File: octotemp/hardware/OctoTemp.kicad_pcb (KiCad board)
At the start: 2 copper layers, 50.5 x 37 mm, 48 parts, among them U1 ESP-12E, U2 SPX3819M5, U3 ADC128D818

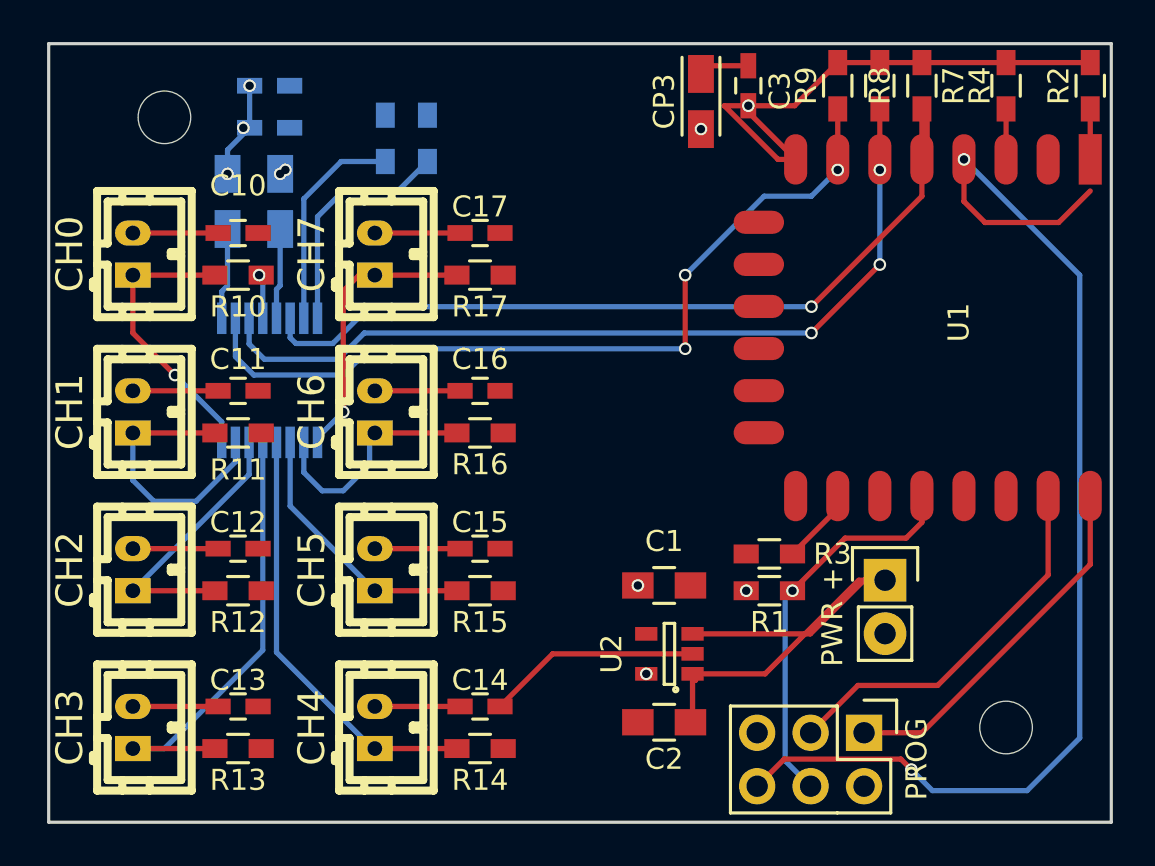
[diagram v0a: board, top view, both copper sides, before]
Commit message: Rearrange board to fit properly in Hammond 1551L.
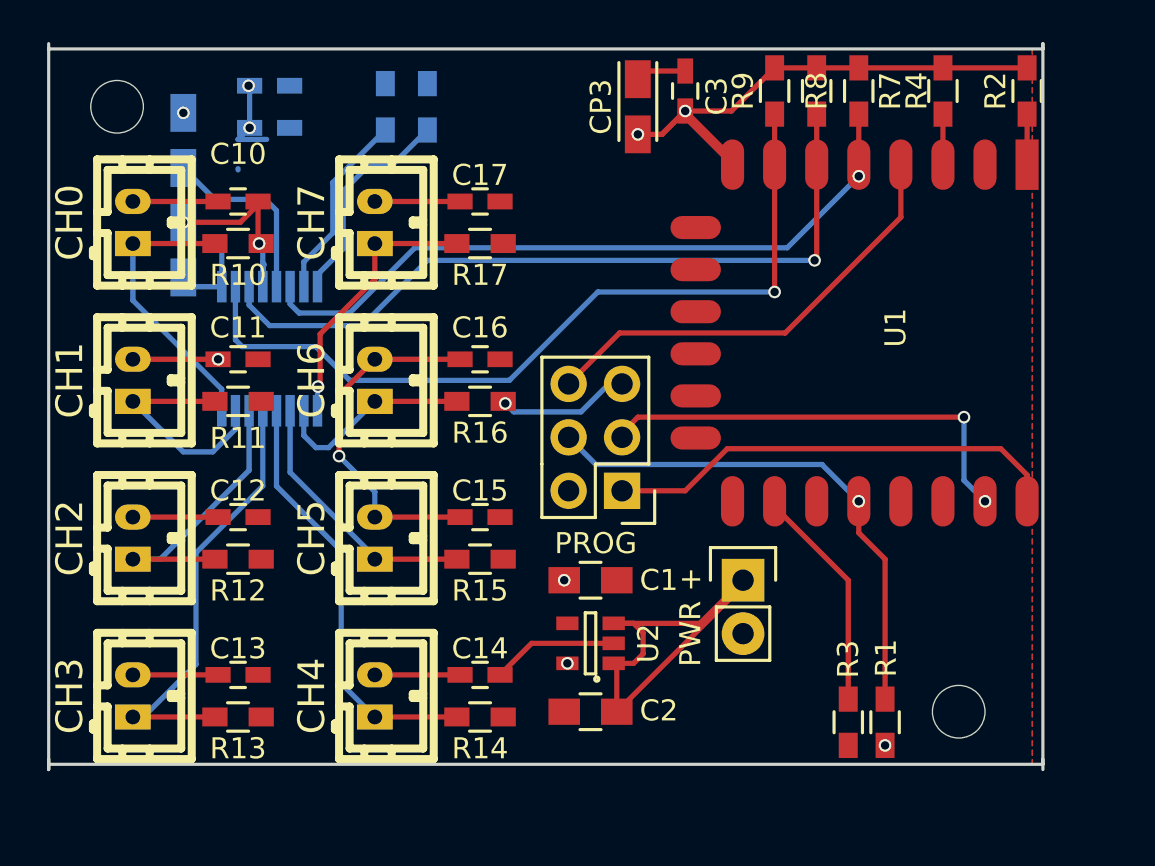
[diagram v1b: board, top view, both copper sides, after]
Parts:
- moved PROG 16.3 mm to (48.0, 41.6), turned to 180 degrees
- moved R3 8.84 mm to (58.8, 52.6), turned to 270 degrees
- moved R1 8.33 mm to (60.5, 52.6), turned to 90 degrees
- moved PWR + 6.75 mm to (53.8, 45.8)
- moved CP1 5.44 mm to (27.1, 24.9)
- moved U2 3.78 mm to (46.5, 48.8)
- moved C2 3.54 mm to (46.5, 52.1)
- moved C1 3.51 mm to (46.5, 45.8)
- moved CP2 3.11 mm to (27.1, 30.1)
- moved C3 3.01 mm to (51.0, 22.6)
- moved CP3 3.01 mm to (48.8, 23.3)
- moved R2 3.01 mm to (67.2, 22.6)
- moved R4 3.01 mm to (63.2, 22.6)
- moved R7 3.01 mm to (59.2, 22.6)
- moved R8 3.01 mm to (57.2, 22.6)
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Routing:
- net ESP_RST: track 58.7 -> 24.0 mm, vias 2 -> 0
- net ADC_VIN: track 67.3 -> 83.2 mm, vias 5 -> 7
- net ADC_GND: track 20.1 -> 30.1 mm
- net Net-(R3-Pad1): track 3.64 -> 10.8 mm
- net ADC_INT: track 40.6 -> 33.8 mm
- net GPIO0: track 19.6 -> 25.0 mm
- net ESP_TXD: track 17.3 -> 21.8 mm
- net SCL: track 40.8 -> 36.4 mm, vias 3 -> 1
- net ESP_RXD: track 18.1 -> 21.2 mm, vias 0 -> 2
- net IN1: track 13.1 -> 11.1 mm
- net +5V: track 24.3 -> 22.3 mm
- net IN6: track 10.9 -> 9.60 mm
- net Net-(R6-Pad2): track 10.3 -> 9.06 mm
- net Net-(R5-Pad2): track 11.1 -> 10.3 mm
- net IN2: track 13.2 -> 14.0 mm
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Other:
- board size 50.5 x 37 mm -> 47.2 x 34.5 mm

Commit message: Fix board outline - try, try again.
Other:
- board size 47.2 x 34.5 mm -> 47.2 x 34 mm
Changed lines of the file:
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@@
     (area 15.514536 18.70288 75.926201 59.0464)
     (thickness 1.6)
-    (drawings 7)
+    (drawings 4)
     (tracks 214)
     (zones 0)
@@
     (pad 1 thru_hole circle (at 0 0) (size 2.5 2.5) (drill 2.5) (layers))
   )
-  (gr_line (start 68 54.578) (end 68 54.328) (angle 90) (layer Edge.Cuts) (width 0.15))
+  (gr_line (start 68 20.578) (end 68 54.578) (angle 90) (layer Edge.Cuts) (width 0.15))
+  (gr_line (start 20.75 20.578) (end 20.75 54.578) (angle 90) (layer Edge.Cuts) (width 0.15))
   (gr_line (start 20.75 54.578) (end 68 54.578) (angle 90) (layer Edge.Cuts) (width 0.15))
   (gr_line (start 20.75 20.578) (end 68 20.578) (angle 90) (layer Edge.Cuts) (width 0.15))
-  (gr_line (start 68 20.328) (end 68 20.578) (angle 90) (layer Edge.Cuts) (width 0.15))
-  (gr_line (start 68 54.828) (end 68 20.328) (angle 90) (layer Edge.Cuts) (width 0.15))
-  (gr_line (start 20.75 20.328) (end 20.75 54.828) (angle 90) (layer Edge.Cuts) (width 0.15))
-  (gr_line (start 20.75 54.828) (end 20.75 54.328) (angle 90) (layer Edge.Cuts) (width 0.15))
   (segment (start 29.75 26.328) (end 29.75 26.268) (width 0.25) (layer B.Cu) (net 0))
   (segment (start 31.575 31.878) (end 31.575 28.253) (width 0.25) (layer B.Cu) (net 1))

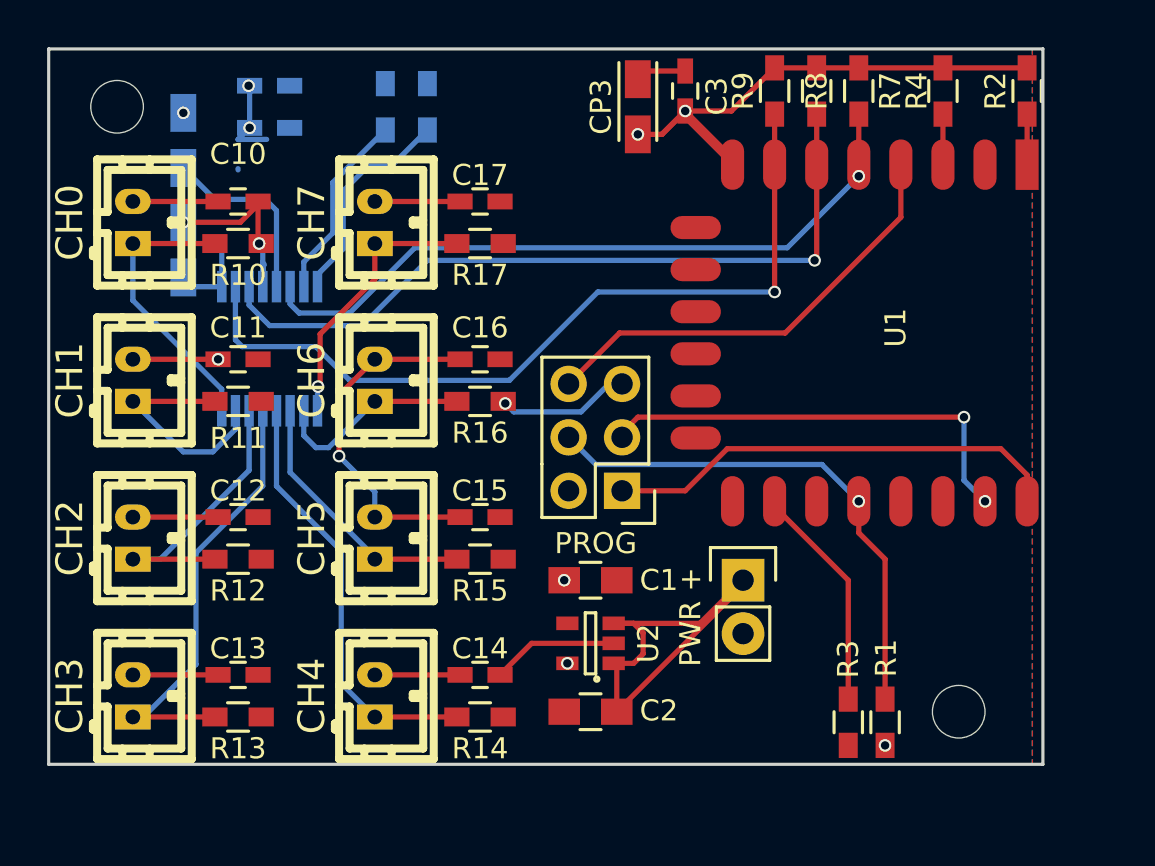
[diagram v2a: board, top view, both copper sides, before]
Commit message: Fix programming header and reset.
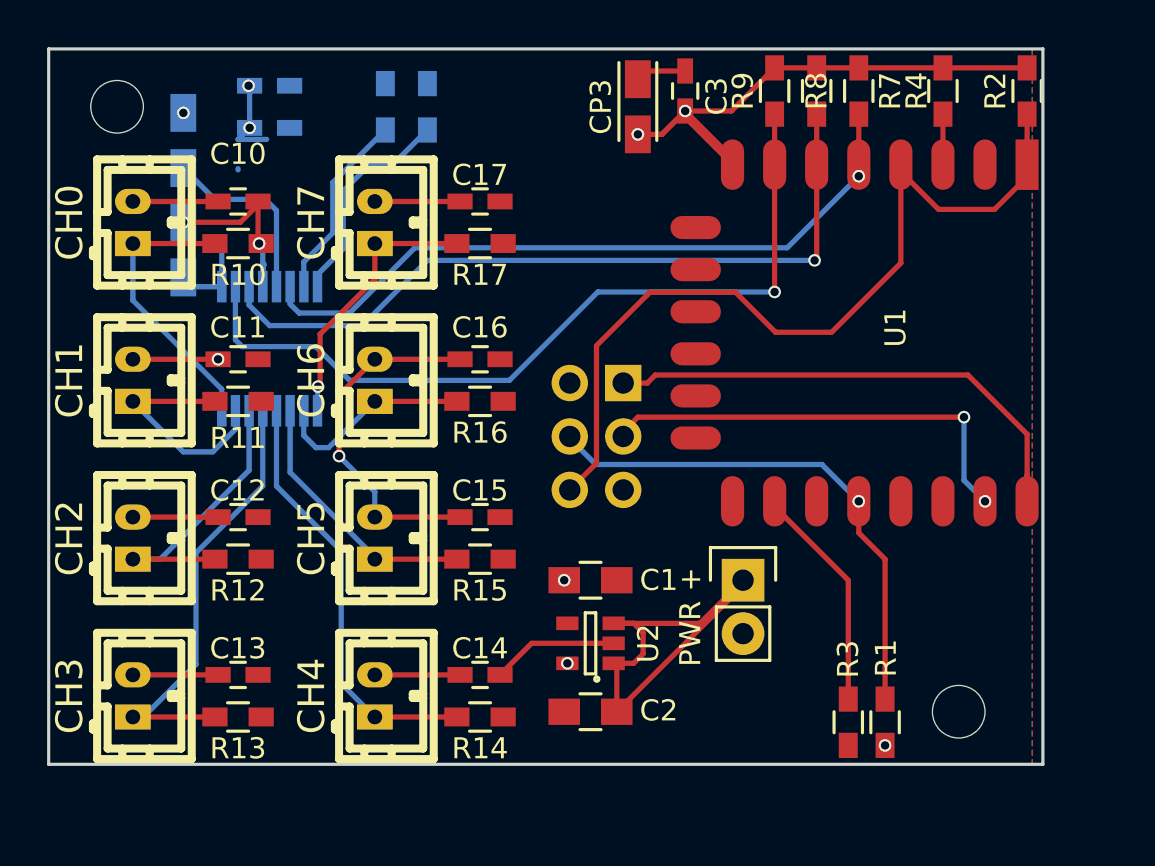
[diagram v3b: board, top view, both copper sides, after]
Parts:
- PROG: moved to B.Cu
- moved PROG 5.12 mm to (48.1, 36.5)
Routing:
- net ESP_RST: track 24.0 -> 40.4 mm
- net ADC_GND: track 30.1 -> 23.6 mm, vias 6 -> 5
- net ESP_TXD: track 21.8 -> 25.0 mm
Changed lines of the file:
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@@
   (general
     (links 100)
-    (no_connects 1)
+    (no_connects 0)
     (area 15.514536 18.70288 75.926201 59.0464)
     (thickness 1.6)
     (drawings 4)
-    (tracks 214)
+    (tracks 219)
     (zones 0)
     (modules 48)
@@
     )
   )
-  (module Pin_Headers:Pin_Header_Straight_2x03 (layer F.Cu)
-    (at 48 41.578 180)
+  (module Pin_Headers:Pin_Header_Straight_2x03 (layer B.Cu)
+    (at 48.055 36.457 180)
     (descr "Through hole pin header")
     (tags "pin header")
-    (fp_text reference PROG (at 1.25 -2.5 180) (layer F.SilkS)
-      (effects (font (size 1 1) (thickness 0.15)))
-    )
-    (fp_text value CONN_02X03 (at 0 -3.1 180) (layer F.Fab)
-      (effects (font (size 1 1) (thickness 0.15)))
-    )
-    (fp_line (start -1.27 1.27) (end -1.27 6.35) (layer F.SilkS) (width 0.15))
-    (fp_line (start -1.55 -1.55) (end 0 -1.55) (layer F.SilkS) (width 0.15))
-    (fp_line (start -1.75 -1.75) (end -1.75 6.85) (layer F.CrtYd) (width 0.05))
-    (fp_line (start 4.3 -1.75) (end 4.3 6.85) (layer F.CrtYd) (width 0.05))
-    (fp_line (start -1.75 -1.75) (end 4.3 -1.75) (layer F.CrtYd) (width 0.05))
-    (fp_line (start -1.75 6.85) (end 4.3 6.85) (layer F.CrtYd) (width 0.05))
-    (fp_line (start 1.27 -1.27) (end 1.27 1.27) (layer F.SilkS) (width 0.15))
-    (fp_line (start 1.27 1.27) (end -1.27 1.27) (layer F.SilkS) (width 0.15))
-    (fp_line (start -1.27 6.35) (end 3.81 6.35) (layer F.SilkS) (width 0.15))
-    (fp_line (start 3.81 6.35) (end 3.81 1.27) (layer F.SilkS) (width 0.15))
-    (fp_line (start -1.55 -1.55) (end -1.55 0) (layer F.SilkS) (width 0.15))
-    (fp_line (start 3.81 -1.27) (end 1.27 -1.27) (layer F.SilkS) (width 0.15))
-    (fp_line (start 3.81 1.27) (end 3.81 -1.27) (layer F.SilkS) (width 0.15))
-    (pad 1 thru_hole rect (at 0 0 180) (size 1.7272 1.7272) (drill 1.016) (layers *.Cu *.Mask F.SilkS)
+    (fp_text reference PROG (at 1.25 2.5 180) (layer B.SilkS)
+      (effects (font (size 1 1) (thickness 0.15)) (justify mirror))
+    )
+    (fp_text value CONN_02X03 (at 0 3.1 180) (layer B.Fab)
+      (effects (font (size 1 1) (thickness 0.15)) (justify mirror))
+    )
+    (fp_line (start -1.27 -1.27) (end -1.27 -6.35) (layer B.SilkS) (width 0.15))
+    (fp_line (start -1.55 1.55) (end 0 1.55) (layer B.SilkS) (width 0.15))
+    (fp_line (start -1.75 1.75) (end -1.75 -6.85) (layer B.CrtYd) (width 0.05))
+    (fp_line (start 4.3 1.75) (end 4.3 -6.85) (layer B.CrtYd) (width 0.05))
+    (fp_line (start -1.75 1.75) (end 4.3 1.75) (layer B.CrtYd) (width 0.05))
+    (fp_line (start -1.75 -6.85) (end 4.3 -6.85) (layer B.CrtYd) (width 0.05))
+    (fp_line (start 1.27 1.27) (end 1.27 -1.27) (layer B.SilkS) (width 0.15))
+    (fp_line (start 1.27 -1.27) (end -1.27 -1.27) (layer B.SilkS) (width 0.15))
+    (fp_line (start -1.27 -6.35) (end 3.81 -6.35) (layer B.SilkS) (width 0.15))
+    (fp_line (start 3.81 -6.35) (end 3.81 -1.27) (layer B.SilkS) (width 0.15))
+    (fp_line (start -1.55 1.55) (end -1.55 0) (layer B.SilkS) (width 0.15))
+    (fp_line (start 3.81 1.27) (end 1.27 1.27) (layer B.SilkS) (width 0.15))
+    (fp_line (start 3.81 -1.27) (end 3.81 1.27) (layer B.SilkS) (width 0.15))
+    (pad 1 thru_hole rect (at 0 0 180) (size 1.7272 1.7272) (drill 1.016) (layers *.Cu *.Mask B.SilkS)
       (net 4 ESP_TXD))
-    (pad 2 thru_hole oval (at 2.54 0 180) (size 1.7272 1.7272) (drill 1.016) (layers *.Cu *.Mask F.SilkS)
-      (net 1 ADC_VIN))
-    (pad 3 thru_hole oval (at 0 2.54 180) (size 1.7272 1.7272) (drill 1.016) (layers *.Cu *.Mask F.SilkS)
+    (pad 2 thru_hole oval (at 2.54 0 180) (size 1.7272 1.7272) (drill 1.016) (layers *.Cu *.Mask B.SilkS)
+      (net 1 ADC_VIN))
+    (pad 3 thru_hole oval (at 0 -2.54 180) (size 1.7272 1.7272) (drill 1.016) (layers *.Cu *.Mask B.SilkS)
       (net 5 ESP_RXD))
-    (pad 4 thru_hole oval (at 2.54 2.54 180) (size 1.7272 1.7272) (drill 1.016) (layers *.Cu *.Mask F.SilkS)
+    (pad 4 thru_hole oval (at 2.54 -2.54 180) (size 1.7272 1.7272) (drill 1.016) (layers *.Cu *.Mask B.SilkS)
       (net 6 GPIO0))
-    (pad 5 thru_hole oval (at 0 5.08 180) (size 1.7272 1.7272) (drill 1.016) (layers *.Cu *.Mask F.SilkS)
-      (net 2 ADC_GND))
-    (pad 6 thru_hole oval (at 2.54 5.08 180) (size 1.7272 1.7272) (drill 1.016) (layers *.Cu *.Mask F.SilkS)
+    (pad 5 thru_hole oval (at 0 -5.08 180) (size 1.7272 1.7272) (drill 1.016) (layers *.Cu *.Mask B.SilkS)
+      (net 2 ADC_GND))
+    (pad 6 thru_hole oval (at 2.54 -5.08 180) (size 1.7272 1.7272) (drill 1.016) (layers *.Cu *.Mask B.SilkS)
       (net 7 ESP_RST))
     (model Pin_Headers.3dshapes/Pin_Header_Straight_2x03.wrl
@@
   (segment (start 30.925 31.878) (end 30.925 30.713) (width 0.25) (layer B.Cu) (net 2))
   (segment (start 30.7 29.678) (end 30.85 29.828) (width 0.25) (layer F.Cu) (net 2))
-  (segment (start 48 36.498) (end 47.38 36.498) (width 0.25) (layer B.Cu) (net 2))
-  (segment (start 47.38 36.498) (end 46.05 37.828) (width 0.25) (layer B.Cu) (net 2))
-  (segment (start 46.05 37.828) (end 42.85 37.828) (width 0.25) (layer B.Cu) (net 2))
-  (segment (start 42.85 37.828) (end 42.45 37.428) (width 0.25) (layer B.Cu) (net 2))
-  (via (at 42.45 37.428) (size 0.6) (drill 0.4) (layers F.Cu B.Cu) (net 2))
-  (segment (start 42.45 37.428) (end 42.35 37.328) (width 0.25) (layer F.Cu) (net 2))
   (segment (start 30.925 31.878) (end 30.925 30.903) (width 0.25) (layer B.Cu) (net 2))
   (segment (start 30.925 30.903) (end 31 30.828) (width 0.25) (layer B.Cu) (net 2))
@@
   (segment (start 53.75 45.828) (end 53.75 46.078) (width 0.25) (layer F.Cu) (net 3))
   (segment (start 53.75 46.078) (end 47.75 52.078) (width 0.25) (layer F.Cu) (net 3))
+  (segment (start 48.055 36.457) (end 49.198 36.457) (width 0.25) (layer F.Cu) (net 4) (status 400000))
+  (segment (start 67.25 38.888) (end 67.25 42.078) (width 0.25) (layer F.Cu) (net 4) (status 800000))
+  (segment (start 64.438 36.076) (end 67.25 38.888) (width 0.25) (layer F.Cu) (net 4))
+  (segment (start 49.579 36.076) (end 64.438 36.076) (width 0.25) (layer F.Cu) (net 4))
+  (segment (start 49.198 36.457) (end 49.579 36.076) (width 0.25) (layer F.Cu) (net 4))
   (segment (start 67.25 42.078) (end 67.25 40.828) (width 0.25) (layer F.Cu) (net 4))
-  (segment (start 51 41.578) (end 48 41.578) (width 0.25) (layer F.Cu) (net 4))
-  (segment (start 53 39.578) (end 51 41.578) (width 0.25) (layer F.Cu) (net 4))
-  (segment (start 66 39.578) (end 53 39.578) (width 0.25) (layer F.Cu) (net 4))
-  (segment (start 67.25 40.828) (end 66 39.578) (width 0.25) (layer F.Cu) (net 4))
   (via (at 65.25 42.078) (size 0.6) (drill 0.4) (layers F.Cu B.Cu) (net 5))
   (segment (start 48 38.828) (end 48.75 38.078) (width 0.25) (layer F.Cu) (net 5))
@@
   (segment (start 64.25 41.078) (end 65.25 42.078) (width 0.25) (layer B.Cu) (net 5))
   (segment (start 48 38.828) (end 48 39.038) (width 0.25) (layer F.Cu) (net 5))
+  (segment (start 46.75 40.328) (end 45.46 39.038) (width 0.25) (layer B.Cu) (net 6))
   (via (at 59.25 42.078) (size 0.6) (drill 0.4) (layers F.Cu B.Cu) (net 6))
   (segment (start 59.25 43.578) (end 60.5 44.828) (width 0.25) (layer F.Cu) (net 6))
   (segment (start 60.5 51.478) (end 60.5 44.828) (width 0.25) (layer F.Cu) (net 6))
   (segment (start 59.25 42.078) (end 59.25 43.578) (width 0.25) (layer F.Cu) (net 6))
-  (segment (start 46.75 40.328) (end 45.46 39.038) (width 0.25) (layer B.Cu) (net 6))
   (segment (start 57.5 40.328) (end 46.75 40.328) (width 0.25) (layer B.Cu) (net 6))
   (segment (start 59.25 42.078) (end 57.5 40.328) (width 0.25) (layer B.Cu) (net 6))
-  (segment (start 61.25 26.078) (end 61.25 28.578) (width 0.25) (layer F.Cu) (net 7))
-  (segment (start 47.88 34.078) (end 45.46 36.498) (width 0.25) (layer F.Cu) (net 7))
-  (segment (start 55.75 34.078) (end 47.88 34.078) (width 0.25) (layer F.Cu) (net 7))
-  (segment (start 61.25 28.578) (end 55.75 34.078) (width 0.25) (layer F.Cu) (net 7))
+  (segment (start 61.25 26.078) (end 61.25 26.411) (width 0.25) (layer F.Cu) (net 7) (status C00000))
+  (segment (start 61.25 26.411) (end 63.041 28.202) (width 0.25) (layer F.Cu) (net 7) (status 400000))
+  (segment (start 65.708 28.202) (end 67.25 26.66) (width 0.25) (layer F.Cu) (net 7) (status 800000))
+  (segment (start 63.041 28.202) (end 65.708 28.202) (width 0.25) (layer F.Cu) (net 7))
+  (segment (start 67.25 26.66) (end 67.25 26.078) (width 0.25) (layer F.Cu) (net 7) (status C00000))
+  (segment (start 45.515 41.537) (end 46.785 40.267) (width 0.25) (layer F.Cu) (net 7) (status 400000))
+  (segment (start 61.25 30.755) (end 61.25 26.078) (width 0.25) (layer F.Cu) (net 7) (status 800000))
+  (segment (start 57.961 34.044) (end 61.25 30.755) (width 0.25) (layer F.Cu) (net 7))
+  (segment (start 55.294 34.044) (end 57.961 34.044) (width 0.25) (layer F.Cu) (net 7))
+  (segment (start 53.389 32.139) (end 55.294 34.044) (width 0.25) (layer F.Cu) (net 7))
+  (segment (start 49.325 32.139) (end 53.389 32.139) (width 0.25) (layer F.Cu) (net 7))
+  (segment (start 49.198 32.266) (end 49.325 32.139) (width 0.25) (layer F.Cu) (net 7))
+  (segment (start 46.785 34.679) (end 49.198 32.266) (width 0.25) (layer F.Cu) (net 7))
+  (segment (start 46.785 40.267) (end 46.785 34.679) (width 0.25) (layer F.Cu) (net 7))
   (segment (start 67.25 26.078) (end 67.25 23.678) (width 0.25) (layer F.Cu) (net 7))
   (segment (start 28.975 37.778) (end 28.975 36.753) (width 0.25) (layer B.Cu) (net 8))
